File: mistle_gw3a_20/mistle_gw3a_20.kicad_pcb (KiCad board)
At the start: 2 copper layers, 90 x 67 mm, 187 parts, among them J1 SWD, J11 Joystick 0, J12 Joystick 1, J13 USB_A_Stacked, J2 USB_C_Receptacle_USB2.0, J3 Jumper block, J4 Micro_SD_Card_Det1, J5 HDMI_A, J6 Grove 1125S-4P, J7 USB_A_Stacked, J8 EXT UART, SW1 Boot, SW2 KEY1, SW3 KEY2, U1 SY8113BADC, U10 74LCX07, U12 CH334R, U13 MT48LC16M16A2TG, U2 W25Q64JVS, U3 USBLC6-2SC6, U4 RP2040, U6 W25Q128JVS, U8 SY8113BADC, U9 74LCX07, Y1 12MHz, Y2 50MHz, Y3 12MHz

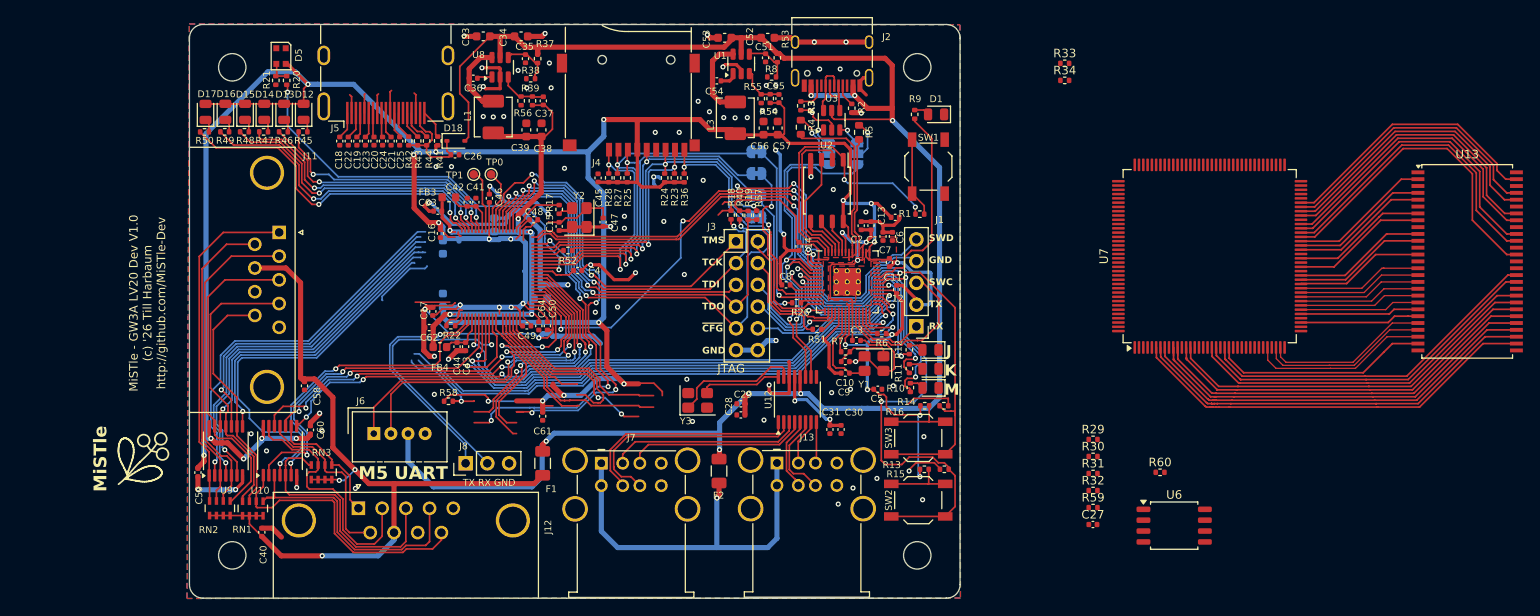
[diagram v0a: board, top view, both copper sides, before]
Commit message: Update gw3a 20 dev board
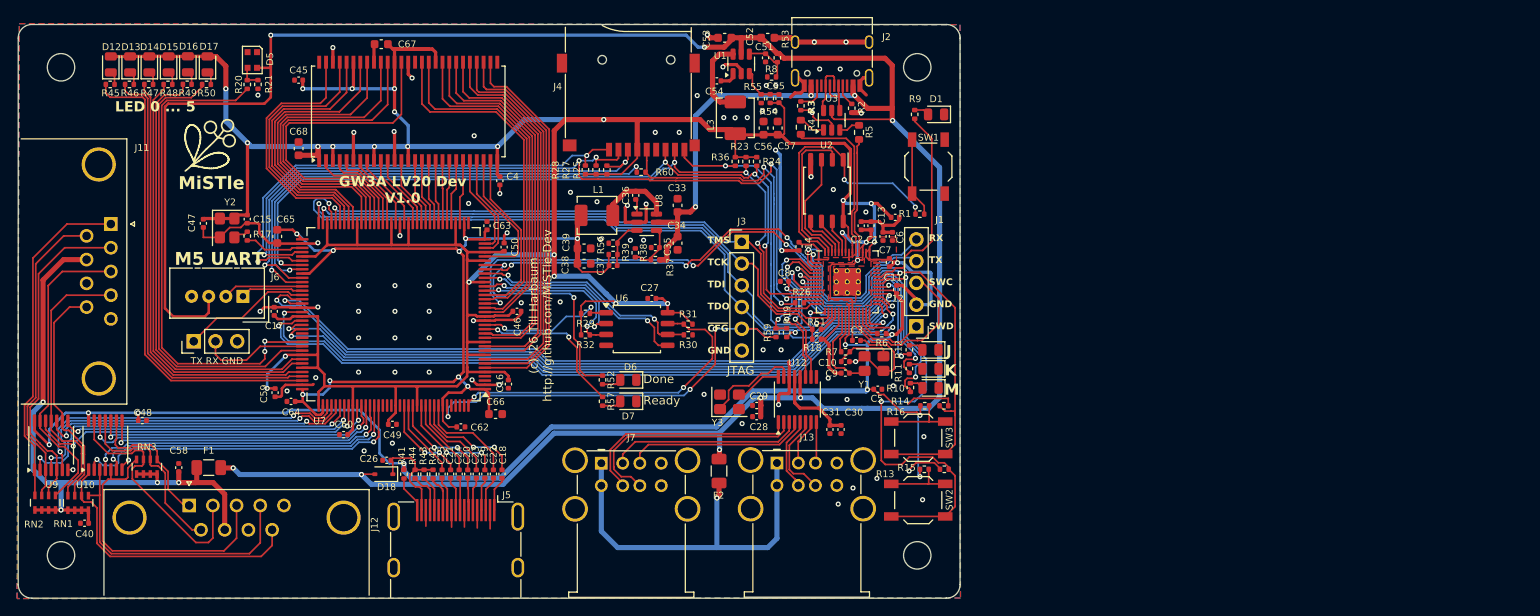
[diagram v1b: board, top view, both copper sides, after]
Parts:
- removed C41, C43: 10uF, Capacitor_SMD:C_0402_1005Metric
- removed C42, C44, C61: 100nF, Capacitor_SMD:C_0402_1005Metric
- removed FB3, FB4: MPZ1608S101, Inductor_SMD:L_0603_1608Metric
- removed JP1: SRC D+, Jumper:SolderJumper-3_P1.3mm_Bridged12_RoundedPad1.0x1.5mm
- removed JP11: DO, Jumper:SolderJumper-2_P1.3mm_Bridged_RoundedPad1.0x1.5mm
- removed JP12: DI, Jumper:SolderJumper-2_P1.3mm_Bridged_RoundedPad1.0x1.5mm
- removed JP13: CLK, Jumper:SolderJumper-2_P1.3mm_Bridged_RoundedPad1.0x1.5mm
- removed JP14: ~{CS}, Jumper:SolderJumper-2_P1.3mm_Bridged_RoundedPad1.0x1.5mm
- removed JP2: SRC D-, Jumper:SolderJumper-3_P1.3mm_Bridged12_RoundedPad1.0x1.5mm
- removed R22: 10k, Resistor_SMD:R_0402_1005Metric
- removed R33, R34, R40, R58: 4k7, Resistor_SMD:R_0402_1005Metric
- removed TP0, TP1: TestPoint, TestPoint:TestPoint_Pad_D1.0mm
- added D6: green, LED_SMD:LED_0805_2012Metric, F.Cu at (151.2, 81.5)
- added D7: green, LED_SMD:LED_0805_2012Metric, F.Cu at (151.2, 84.0)
- C65, C66, C67, C68: moved to F.Cu
- J3: value Jumper block -> JTAG; footprint Connector_PinHeader_2.54mm:PinHeader_2x06_P2.54mm_Vertical -> Connector_PinHeader_2.54mm:PinHeader_1x06_P2.54mm_Vertical
- R52: value 22 -> 560
- moved U13 124.9 mm to (125.6, 50.2), turned to 90 degrees
- moved U7 95.6 mm to (123.8, 73.8), turned to 180 degrees
- moved R60 70.0 mm to (152.8, 57.2)
- moved U6 66.8 mm to (152.3, 75.6)
- moved R32 62.0 mm to (146.2, 76.2), turned to 180 degrees
- moved R29 61.1 mm to (146.2, 73.8), turned to 180 degrees
- moved C27 57.9 mm to (154.0, 72.0), turned to 180 degrees
- moved J5 53.6 mm to (131.1, 100.0), turned to -90 degrees
- moved C48 51.4 mm to (94.5, 86.2)
- moved R31 50.4 mm to (158.2, 75.0)
- moved R30 49.4 mm to (158.2, 76.2), turned to 180 degrees
- moved C47 46.7 mm to (101.6, 63.2), turned to 90 degrees
- moved C18 43.2 mm to (136.5, 92.5), turned to -90 degrees
- moved C22 42.4 mm to (135.5, 92.5), turned to -90 degrees
- moved R59 42.3 mm to (168.5, 76.0), turned to -90 degrees
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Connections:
- net +1V1 renamed +1.1V
- net /GW3A-LV20 FPGA/GW3A LV20 memory/A0 renamed /GW3A-LV20 FPGA/GW3A LV20 memory/SDR_A0
- net /GW3A-LV20 FPGA/GW3A LV20 memory/A1 renamed /GW3A-LV20 FPGA/GW3A LV20 memory/SDR_A1
- net /GW3A-LV20 FPGA/GW3A LV20 memory/A2 renamed /GW3A-LV20 FPGA/GW3A LV20 memory/SDR_A2
- net /GW3A-LV20 FPGA/Interfaces/SD_CMD renamed SD_CMD
- net /GW3A-LV20 FPGA/Interfaces/SD_DAT2 renamed SD_DAT2
- net CK+ renamed /GW3A-LV20 FPGA/Interfaces/CK+
- net CK- renamed /GW3A-LV20 FPGA/Interfaces/CK-
- net CLK50 renamed /GW3A-LV20 FPGA/Interfaces/CLK50
- net D0+ renamed /GW3A-LV20 FPGA/Interfaces/D0+
- net D0- renamed /GW3A-LV20 FPGA/Interfaces/D0-
- net D1+ renamed /GW3A-LV20 FPGA/Interfaces/D1+
- net D1- renamed /GW3A-LV20 FPGA/Interfaces/D1-
- net D2+ renamed /GW3A-LV20 FPGA/Interfaces/D2+
- net D2- renamed /GW3A-LV20 FPGA/Interfaces/D2-
- net JOYA0 renamed /GW3A-LV20 FPGA/Interfaces/JOYA0
- net JOYA1 renamed /GW3A-LV20 FPGA/Interfaces/JOYA1
- net JOYA2 renamed /GW3A-LV20 FPGA/Interfaces/JOYA2
- net JOYA3 renamed /GW3A-LV20 FPGA/Interfaces/JOYA3
- net JOYA4 renamed /GW3A-LV20 FPGA/Interfaces/JOYA4
- net JOYA5 renamed /GW3A-LV20 FPGA/Interfaces/JOYA5
- net JOYB0 renamed /GW3A-LV20 FPGA/Interfaces/JOYB0
- net JOYB1 renamed /GW3A-LV20 FPGA/Interfaces/JOYB1
- net JOYB2 renamed /GW3A-LV20 FPGA/Interfaces/JOYB2
- net JOYB3 renamed /GW3A-LV20 FPGA/Interfaces/JOYB3
- net JOYB4 renamed /GW3A-LV20 FPGA/Interfaces/JOYB4
- net JOYB5 renamed /GW3A-LV20 FPGA/Interfaces/JOYB5
- net LED2 renamed /GW3A-LV20 FPGA/Interfaces/LED2
- net LED3 renamed /GW3A-LV20 FPGA/Interfaces/LED3
- net LED4 renamed /GW3A-LV20 FPGA/Interfaces/LED4
- net LED5 renamed /GW3A-LV20 FPGA/Interfaces/LED5
- net Net-(RN1-R1.1) renamed /GW3A-LV20 FPGA/Interfaces/RIGHT-1
- net Net-(RN1-R1.2) renamed /GW3A-LV20 FPGA/Interfaces/Vjs
- net Net-(RN1-R2.1) renamed /GW3A-LV20 FPGA/Interfaces/BTN2-1
- net Net-(RN1-R3.1) renamed /GW3A-LV20 FPGA/Interfaces/BTN2-0
- net Net-(RN1-R4.1) renamed /GW3A-LV20 FPGA/Interfaces/RIGHT-0
- net Net-(RN2-R1.1) renamed /GW3A-LV20 FPGA/Interfaces/LEFT-0
- net Net-(RN2-R2.1) renamed /GW3A-LV20 FPGA/Interfaces/DOWN-0
- net Net-(RN2-R3.1) renamed /GW3A-LV20 FPGA/Interfaces/BTN1-0
- net Net-(RN2-R4.1) renamed /GW3A-LV20 FPGA/Interfaces/UP-0
- net Net-(RN3-R1.1) renamed /GW3A-LV20 FPGA/Interfaces/UP-1
- net Net-(RN3-R2.1) renamed /GW3A-LV20 FPGA/Interfaces/BTN1-1
- net Net-(RN3-R3.1) renamed /GW3A-LV20 FPGA/Interfaces/DOWN-1
- net Net-(RN3-R4.1) renamed /GW3A-LV20 FPGA/Interfaces/LEFT-1
- C11 pad 1: +3V3 -> +3.3V
- C12 pad 1: +3V3 -> +3.3V
- C13 pad 1: +3V3 -> +3.3V
- C14 pad 1: +3V3 -> +3.3V
- C15 pad 1: +3V3 -> +3.3V
- C16 pad 2: +3V3 -> +3.3V
- C17 pad 2: +3V3 -> +3.3V
- C37 pad 2: +1V0 -> +0.9V
- C38 pad 1: +1V0 -> +0.9V
- C39 pad 1: +1V0 -> +0.9V
- C4 pad 2: +3V3 -> +3.3V
- C45 pad 2: +3V3 -> +3.3V
- C46 pad 2: +3V3 -> +3.3V
- C47 pad 2: +3V3 -> +3.3V
- C48 pad 2: +3V3 -> +3.3V
- C49 pad 2: +3V3 -> +3.3V
- C5 pad 1: +3V3 -> +3.3V
- C50 pad 2: +3V3 -> +3.3V
- C55 pad 2: +3V3 -> +3.3V
- C56 pad 1: +3V3 -> +3.3V
- C57 pad 1: +3V3 -> +3.3V
- C59 pad 2: +3V3 -> +3.3V
- C6 pad 2: +3V3 -> +3.3V
- C60 pad 2: +3V3 -> +3.3V
- C62 pad 1: +1V0 -> +0.9V
- C63 pad 2: +1V0 -> +0.9V
- C64 pad 2: +1V0 -> +0.9V
- C65 pad 1: +1V0 -> +0.9V
- C66 pad 1: +1V0 -> +0.9V
- C67 pad 1: +3V3 -> +3.3V
- C68 pad 1: +3V3 -> +3.3V
- C7 pad 1: +3V3 -> +3.3V
- C8 pad 1: +3V3 -> +3.3V
- D12 pad 2: +3V3 -> +3.3V
- D13 pad 2: +3V3 -> +3.3V
- D14 pad 2: +3V3 -> +3.3V
- D15 pad 2: +3V3 -> +3.3V
- D16 pad 2: +3V3 -> +3.3V
- D17 pad 2: +3V3 -> +3.3V
- D5 pad 4: +3V3 -> +5V
- J3 pad 1: Net-(J3-Pin_1) -> TMS
- J3 pad 2: TMS -> TCK
- J3 pad 3: Net-(J3-Pin_3) -> TDI
- J3 pad 4: TCK -> TDO
- J3 pad 5: Net-(J3-Pin_5) -> ~{CFG}
- J3 pad 6: TDI -> GND
- J4 pad 2: /GW3A-LV20 FPGA/Interfaces/SD_DAT3 -> SD_DAT3
- J4 pad 4: +3V3 -> +3.3V
- J4 pad 7: /GW3A-LV20 FPGA/Interfaces/SD_DAT0 -> SD_DAT0
- J4 pad 8: /GW3A-LV20 FPGA/Interfaces/SD_DAT1 -> SD_DAT1
- L1 pad 2: +1V0 -> +0.9V
- L3 pad 2: +3V3 -> +3.3V
- R13 pad 1: +3V3 -> +3.3V
- R14 pad 1: +3V3 -> +3.3V
- R15 pad 1: KEY0 -> MODE0
- R16 pad 1: KEY1 -> MODE1
- R18 pad 1: Net-(J3-Pin_3) -> TCK
- R19 pad 1: +3V3 -> +3.3V
- R19 pad 2: Net-(J3-Pin_7) -> TDO
- R23 pad 1: +3V3 -> +3.3V
- R23 pad 2: /GW3A-LV20 FPGA/Interfaces/SD_DAT1 -> SD_DAT1
- R24 pad 1: +3V3 -> +3.3V
- R24 pad 2: /GW3A-LV20 FPGA/Interfaces/SD_DAT0 -> SD_DAT0
- R25 pad 1: +3V3 -> +3.3V
- R26 pad 1: Net-(JP13-A) -> /GW3A-LV20 FPGA/Interfaces/SD_CLK
- R27 pad 1: +3V3 -> +3.3V
- R27 pad 2: /GW3A-LV20 FPGA/Interfaces/SD_DAT3 -> SD_DAT3
- R28 pad 1: +3V3 -> +3.3V
- R36 pad 1: +3V3 -> +3.3V
- R39 pad 2: +1V0 -> +0.9V
- R4 pad 1: Net-(JP1-C) -> Net-(R4-Pad1)
- R41 pad 1: +3V3 -> +3.3V
- R45 pad 1: LED0 -> /GW3A-LV20 FPGA/Interfaces/LED0
- R46 pad 1: LED1 -> /GW3A-LV20 FPGA/Interfaces/LED1
- R5 pad 1: Net-(JP2-C) -> Net-(R5-Pad1)
- R52 pad 1: /GW3A-LV20 FPGA/Interfaces/SD_CLK -> /GW3A-LV20 FPGA/GW3A LV20 memory/DONE
- R52 pad 2: SD_CLK -> Net-(D6-A)
- R54 pad 2: +3V3 -> +3.3V
- R57 pad 1: DBG RX -> /GW3A-LV20 FPGA/GW3A LV20 memory/READY
- R57 pad 2: /UART_TX -> Net-(D7-A)
- R59 pad 2: CLK -> ~{CFG}
- R6 pad 1: +3V3 -> +3.3V
- SW2 pad 2: KEY0 -> MODE0
- SW3 pad 2: KEY1 -> MODE1
- U10 pad 14: +3V3 -> +3.3V
- U2 pad 8: +3V3 -> +3.3V
- U3 pad 1: Net-(JP1-A) -> Net-(R4-Pad1)
- U3 pad 3: Net-(JP2-A) -> Net-(R5-Pad1)
- U4 pad 1: +3V3 -> +3.3V
- U4 pad 10: +3V3 -> +3.3V
- U4 pad 11: SD_DO -> SD_DAT0
- U4 pad 12: ~{SD_CS} -> SD_DAT3
- U4 pad 14: SD_DI -> SD_DAT1
- U4 pad 22: +3V3 -> +3.3V
- U4 pad 33: +3V3 -> +3.3V
- U4 pad 42: +3V3 -> +3.3V
- U4 pad 43: +3V3 -> +3.3V
- U4 pad 44: +3V3 -> +3.3V
- U4 pad 48: +3V3 -> +3.3V
- U4 pad 49: +3V3 -> +3.3V
- U7 pad 1: unconnected-(U7A-VCC-Pad1) -> +0.9V
- U7 pad 100: unconnected-(U7A-VCCIO7-Pad100) -> +3.3V
- U7 pad 103: unconnected-(U7A-VCCIO7-Pad103) -> +3.3V
- U7 pad 105: LED0 -> /GW3A-LV20 FPGA/Interfaces/LED1
- U7 pad 106: LED1 -> /GW3A-LV20 FPGA/Interfaces/LED0
- U7 pad 108: unconnected-(U7A-VCC-Pad108) -> +0.9V
- U7 pad 109: unconnected-(U7A-VCCIO10_VCCX-Pad109) -> +3.3V
- U7 pad 110: unconnected-(U7A-VCC-Pad110) -> +0.9V
- U7 pad 117: unconnected-(U7A-VCCIO6-Pad117) -> +3.3V
- U7 pad 12: unconnected-(U7A-VCCIO4-Pad12) -> +3.3V
- U7 pad 127: unconnected-(U7A-VCCIO6-Pad127) -> +3.3V
- U7 pad 132: unconnected-(U7A-VCCIO6-Pad132) -> +3.3V
- U7 pad 138: unconnected-(U7A-VCC-Pad138) -> +0.9V
- U7 pad 139: CLK -> ~{CFG}
- U7 pad 18: unconnected-(U7A-VCCIO4-Pad18) -> +3.3V
- U7 pad 21: /GW3A-LV20 FPGA/GW3A LV20 memory/MODE0 -> MODE1
- U7 pad 26: unconnected-(U7A-VCCIO4-Pad26) -> +3.3V
- U7 pad 29: /GW3A-LV20 FPGA/GW3A LV20 memory/MODE0 -> MODE0
- U7 pad 31: unconnected-(U7A-VCCIO3-Pad31) -> +3.3V
- U7 pad 33: unconnected-(U7A-VCCIO3-Pad33) -> +3.3V
- U7 pad 36: unconnected-(U7A-VCC-Pad36) -> +0.9V
- U7 pad 38: unconnected-(U7A-VCC-Pad38) -> +0.9V
- U7 pad 4: ~{RESET} -> unconnected-(U7H-IOB12B/GCLKC_10B/RDWR_B/LPLL1_C_IN0-Pad4)
- U7 pad 40: unconnected-(U7A-VCCIO10_VCCX-Pad40) -> +3.3V
- U7 pad 5: unconnected-(U7A-VCCIO5-Pad5) -> +3.3V
- U7 pad 51: unconnected-(U7A-VCCIO2-Pad51) -> +3.3V
- U7 pad 55: unconnected-(U7A-VCCIO2-Pad55) -> +3.3V
- U7 pad 63: unconnected-(U7A-VCCIO2-Pad63) -> +3.3V
- U7 pad 68: Net-(J3-Pin_1) -> TMS
- U7 pad 69: Net-(J3-Pin_7) -> TDO
- U7 pad 70: unconnected-(U7A-VCCIO10_VCCX-Pad70) -> +3.3V
- U7 pad 71: Net-(J3-Pin_3) -> TCK
- U7 pad 72: Net-(J3-Pin_5) -> TDI
- U7 pad 73: unconnected-(U7A-VCC-Pad73) -> +0.9V
- U7 pad 76: /GW3A-LV20 FPGA/Interfaces/SD_DAT3 -> SD_DAT3
- U7 pad 77: unconnected-(U7A-VCCIO1-Pad77) -> +3.3V
- U7 pad 79: /GW3A-LV20 FPGA/Interfaces/SD_DAT1 -> SD_DAT1
- U7 pad 80: /GW3A-LV20 FPGA/Interfaces/SD_DAT0 -> SD_DAT0
- U7 pad 81: unconnected-(U7A-VCC-Pad81) -> +0.9V
- U7 pad 9: unconnected-(U7A-VCCIO5-Pad9) -> +3.3V
- U7 pad 91: unconnected-(U7A-VCCIO0-Pad91) -> +3.3V
- U7 pad 96: ~{USER} -> unconnected-(U7J-IOT27B-Pad96)
- U9 pad 14: +3V3 -> +3.3V
- Y2 pad 1: +3V3 -> +3.3V
- Y2 pad 4: +3V3 -> +3.3V
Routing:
- net +3.3V: track 0.00 -> 587.1 mm, vias 0 -> 33
- net +3V3: track 455.1 -> 0.00 mm, vias 30 -> 0
- net (no net): track 277.6 -> 0.00 mm, vias 18 -> 0
- net +0.9V: track 0.00 -> 120.2 mm, vias 0 -> 9
- net +5V: track 216.6 -> 331.0 mm, vias 7 -> 11
- net SD_DAT3: track 0.00 -> 102.8 mm, vias 0 -> 5
- net SD_DAT1: track 0.00 -> 93.0 mm, vias 0 -> 4
- net SD_DAT0: track 0.00 -> 93.0 mm, vias 0 -> 4
- net GND: track 283.9 -> 201.2 mm, vias 82 -> 83
- net TDO: track 11.2 -> 78.4 mm, vias 1 -> 3
- net +1V0: track 65.8 -> 0.00 mm, vias 5 -> 0
- net SD_CMD: track 0.00 -> 61.0 mm, vias 0 -> 2
- net TDI: track 12.4 -> 72.0 mm, vias 1 -> 2
- net Net-(U7D-IOT61A/GCLKT_2): track 0.00 -> 57.2 mm, vias 0 -> 2
- net TCK: track 12.2 -> 67.6 mm, vias 0 -> 1
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- added copper zone on F.Cu, net +3.3V
- removed copper zone on F.Cu, net +3V3
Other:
- board size 90 x 67 mm -> 110 x 67 mm
- board text added: "(c) '26 Till Harbaum http://github.com/MiSTle-Dev"
- board text added: "Done"
- board text added: "GW3A LV20 Dev V1.0"
- board text added: "LED 0 ... 5"
- board text added: "RX TX SWC GND SWD"
- board text added: "Ready"
- board text removed: "MiSTle - GW3A LV20 Dev V1.0 (c) '26 Till Harbaum http://github.com/MiSTle-Dev"
- board text removed: "PIO native"
- board text removed: "SDC"
- board text removed: "SWD GND SWC TX RX"
- board text removed: "USB"

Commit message: Update gw3a dev board
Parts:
- C65, C66, C67, C68: footprint Capacitor_SMD:C_0603_1608Metric -> Capacitor_SMD:C_0402_1005Metric
- U2: footprint Package_SO:SOIC-8_5.23x5.23mm_P1.27mm -> Package_SO:SOIC-8_5.3x5.3mm_P1.27mm
- U6: value W25Q128JVS -> W25Q64JVS
- U7: value ~ -> GW3A-LV20-Q144
- moved R23 18.8 mm to (146.2, 57.0), turned to 90 degrees
- moved R25 15.8 mm to (164.5, 58.2), turned to -90 degrees
- moved R36 2.40 mm to (162.8, 58.2)
- moved R24 2.21 mm to (166.0, 58.2)
- moved R27 1.41 mm to (148.9, 57.0)
- moved R28 1.36 mm to (147.6, 57.0)
- moved SW1 1.18 mm to (185.1, 56.6), turned to 0 degrees
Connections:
- U4 pad 14: SD_DAT1 -> SD_CMD
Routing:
- net SD_CMD: track 61.0 -> 96.6 mm, vias 2 -> 5
- net SD_DAT1: track 93.0 -> 66.4 mm, vias 4 -> 3
- net ~{SD_DET}: track 44.3 -> 29.7 mm
- net SD_DAT3: track 102.8 -> 95.4 mm
- net Net-(U4-GPIO25): track 23.9 -> 28.1 mm
- net +3.3V: track 587.1 -> 590.6 mm
- net /GW3A-LV20 FPGA/Interfaces/SD_CLK: track 36.8 -> 33.3 mm
- net GND: track 201.2 -> 204.6 mm
- net Net-(U7D-IOT61A/GCLKT_2): track 57.2 -> 55.6 mm
- net SD_DAT0: track 93.0 -> 91.6 mm
- net MODE0: track 113.2 -> 114.2 mm
- net MODE1: track 102.6 -> 103.5 mm
- net /~{USB_BOOT}: track 9.53 -> 10.2 mm

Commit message: Update gw3a board
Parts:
- removed D7: green, LED_SMD:LED_0805_2012Metric
- removed R52, R57: 560, Resistor_SMD:R_0402_1005Metric
- added R22: 1k, Resistor_SMD:R_0402_1005Metric, F.Cu at (108.4, 75.5)
- added R61: 4k7, Resistor_SMD:R_0402_1005Metric, F.Cu at (138.5, 75.5)
- added R62: 4k7, Resistor_SMD:R_0402_1005Metric, F.Cu at (145.3, 72.6)
- moved D6 4.76 mm to (146.6, 80.5)
- moved C59 3.91 mm to (110.2, 79.1)
- moved C11 1.62 mm to (182.0, 66.2), turned to 0 degrees
- moved C46 0.89 mm to (138.5, 74.3), turned to 0 degrees
- moved C49 0.40 mm to (124.1, 86.7), turned to 90 degrees
- moved C66 0.30 mm to (135.4, 85.5)
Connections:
- D6 pad 2: Net-(D6-A) -> /GW3A-LV20 FPGA/GW3A LV20 memory/DONE
- U7 pad 95: unconnected-(U7C-IOT29A/PUDC_B-Pad95) -> Net-(U7C-IOT29A/PUDC_B)
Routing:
- net /GW3A-LV20 FPGA/GW3A LV20 memory/READY: track 18.9 -> 3.68 mm, vias 2 -> 0
- net GND: track 204.6 -> 192.3 mm, vias 83 -> 88
- net Net-(U7C-IOT29A/PUDC_B): track 0.00 -> 5.04 mm
- net MODE1: track 103.5 -> 107.3 mm
- net +3.3V: track 590.6 -> 587.2 mm, vias 33 -> 31
- net /GW3A-LV20 FPGA/GW3A LV20 memory/DONE: track 27.6 -> 24.9 mm
- net Net-(D6-A): track 2.28 -> 0.00 mm
- net Net-(D7-A): track 2.27 -> 0.00 mm
- net ~{CS}: track 77.9 -> 78.9 mm
- net /GW3A-LV20 FPGA/GW3A LV20 memory/SDR_DQ9: track 37.2 -> 36.2 mm
- net /GW3A-LV20 FPGA/GW3A LV20 memory/SDR_DQ8: track 39.2 -> 38.1 mm
- net /GW3A-LV20 FPGA/GW3A LV20 memory/SDR_DQ11: track 35.0 -> 34.0 mm
- net /GW3A-LV20 FPGA/GW3A LV20 memory/SDR_DQ0: track 11.3 -> 10.3 mm
- net /GW3A-LV20 FPGA/GW3A LV20 memory/SDR_DQ10: track 36.5 -> 35.5 mm
- net MISO: track 84.8 -> 85.8 mm
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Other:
- board text removed: "Ready"

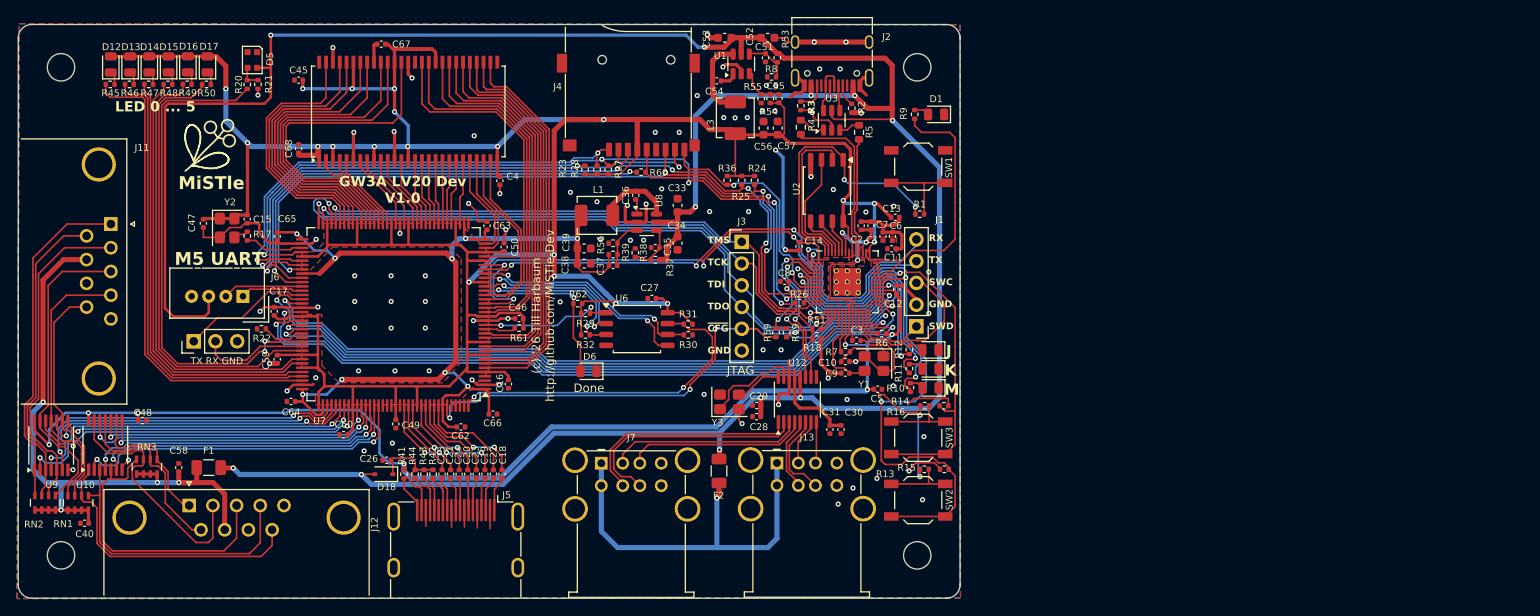
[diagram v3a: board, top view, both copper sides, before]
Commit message: Update mistle-gw3a board for rp2350
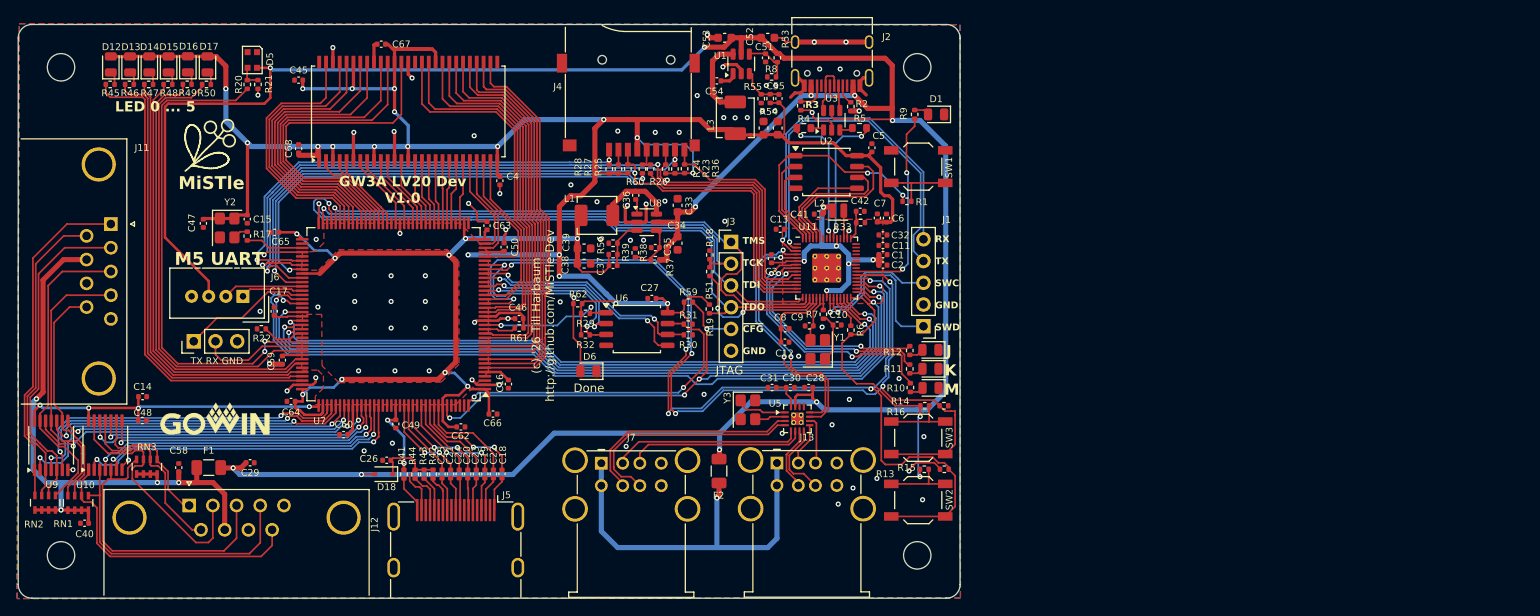
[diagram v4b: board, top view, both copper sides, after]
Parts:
- removed U12: CH334R, Package_SO:QSOP-16_3.9x4.9mm_P0.635mm
- removed U4: RP2040, Sleep-Lib:RP2040-QFN-56
- added C32: 4.7u, Capacitor_SMD:C_0402_1005Metric, F.Cu at (181.0, 64.6)
- added C41: 4.7u, Capacitor_SMD:C_0402_1005Metric, F.Cu at (173.4, 62.1)
- added C42: 4.7u, Capacitor_SMD:C_0402_1005Metric, F.Cu at (178.3, 61.8)
- added L2: 3.3u, Inductor_SMD:L_Changjiang_FTC201610D, F.Cu at (175.8, 61.7)
- added R33: 33, Resistor_SMD:R_0402_1005Metric, F.Cu at (178.4, 63.1)
- added U11: RP2350_60QFN, RP2350_60QFN_minimal:RP2350-QFN-60-1EP_7x7_P0.4mm_EP3.4x3.4mm_ThermalVias, F.Cu at (174.4, 68.5)
- added U5: CH334P, Package_DFN_QFN:QFN-16-1EP_3x3mm_P0.5mm_EP1.45x1.45mm_ThermalVias, F.Cu at (171.0, 86.1)
- R10, R11, R12, R45, R46, R47, R48, R49, R50, R9: value 560 -> 1k
- moved C14 78.7 mm to (94.5, 83.5), turned to 0 degrees
- moved C29 59.5 mm to (107.1, 91.2), turned to 180 degrees
- moved C5 28.2 mm to (179.7, 54.4), turned to 90 degrees
- moved R26 23.4 mm to (153.8, 56.9), turned to -90 degrees
- moved R18 15.9 mm to (160.8, 66.9), turned to 90 degrees
- moved C12 14.4 mm to (169.6, 77.1), turned to 0 degrees
- moved R51 14.2 mm to (160.8, 68.9), turned to 90 degrees
- moved C3 13.8 mm to (168.0, 67.3), turned to 90 degrees
- moved C13 13.5 mm to (169.0, 63.9), turned to 180 degrees
- moved R25 13.4 mm to (151.2, 56.9), turned to 90 degrees
- moved R59 10.8 mm to (158.3, 72.4), turned to 0 degrees
- moved R23 10.5 mm to (156.7, 56.9)
- moved R24 10.5 mm to (155.6, 56.9), turned to 90 degrees
- moved R19 9.44 mm to (160.7, 73.2)
- moved C31 8.35 mm to (168.0, 82.4), turned to 0 degrees
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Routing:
- net +3.3V: track 587.2 -> 382.5 mm, vias 31 -> 27
- net GND: track 192.3 -> 81.4 mm, vias 88 -> 81
- net /GW3A-LV20 FPGA/Interfaces/SD_CLK: track 33.3 -> 3.17 mm, vias 2 -> 0
- net SD_CLK_PI: track 1.73 -> 28.8 mm
- net DBG TX: track 22.1 -> 43.5 mm
- net DBG RX: track 24.8 -> 42.2 mm
- net Net-(U11-GPIO15): track 3.00 -> 17.3 mm, vias 0 -> 2
- net +5V: track 331.0 -> 317.3 mm, vias 11 -> 10
- net Net-(U11-QSPI_SD3): track 4.09 -> 17.3 mm
- net ~{IRQ}: track 83.6 -> 95.9 mm
- net Net-(U11-QSPI_SCLK): track 4.45 -> 15.3 mm
- net TCK: track 67.6 -> 56.9 mm
- net USB D-: track 18.8 -> 29.5 mm
- net ~{CFG}: track 69.0 -> 79.0 mm, vias 4 -> 5
- net SWD: track 10.5 -> 20.0 mm, vias 0 -> 1
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- removed copper zone on F.Cu, net +1.1V
